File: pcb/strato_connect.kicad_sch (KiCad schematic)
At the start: 42 parts, among them J1 Conn_Coaxial, J2 Conn_02x03_Odd_Even, J3 Conn_01x04_Pin, J4 Conn_01x02_Pin, J5 Conn_01x05_Pin, SW1 SW_SPST, SW2 SW_SPST, U1 TPS565242, U2 ATmega328PB-A, U4 RF4463F30, Y1 CSTNE16M0V530000R0

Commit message: rough layout of the rev2 pcb
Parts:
- removed U2: ATmega328PB-A, Package_QFP:TQFP-32_7x7mm_P0.8mm, symbol MCU_Microchip_ATmega:ATmega328PB-A
- added U2: ATmega328PB-M, Package_DFN_QFN:QFN-32-1EP_5x5mm_P0.5mm_EP3.1x3.1mm, symbol MCU_Microchip_ATmega:ATmega328PB-M
- C11, C9: footprint Capacitor_SMD:CP_Elec_5x5.3 -> Capacitor_SMD:C_0603_1608Metric
- J2: footprint Connector_PinHeader_2.54mm:PinHeader_2x03_P2.54mm_Vertical -> Connector_PinHeader_2.54mm:PinHeader_2x03_P2.54mm_Vertical_SMD
- J3: footprint (none) -> Connector_JST:JST_SH_SM04B-SRSS-TB_1x04-1MP_P1.00mm_Horizontal
- J4: footprint Connector_JST:JST_SH_BM04B-SRSS-TB_1x04-1MP_P1.00mm_Vertical -> Connector_JST:JST_PH_S2B-PH-SM4-TB_1x02-1MP_P2.00mm_Horizontal
- J5: footprint (none) -> Connector_JST:JST_SH_SM05B-SRSS-TB_1x05-1MP_P1.00mm_Horizontal
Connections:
- net +5V: now also U2.18 (AVCC), U2.20 (AREF), U2.4 (VCC)
- net GND: now also U2.21 (GND), U2.33 (GND), U2.5 (GND)
- net LED_RX: now also U2.25 (PC2)
- net LED_TX: now also U2.26 (PC3)
- net SCL: now also U2.28 (PC5)
- net SDA: now also U2.27 (PC4)
- net SPI_MISO: now also U2.16 (PB4)
- net SPI_MOSI: now also U2.15 (PB3)
- net SPI_SCK: now also U2.17 (PB5)
- net ~{INT}: now also U2.24 (PC1)
- net ~{IRQ}: now also U2.32 (PD2)
- net ~{RST}: now also U2.29 (~{RESET}/PC6)
- net ~{SDN}: now also U2.13 (PB1)
- net ~{SPI_CS}: now also U2.14 (PB2)
- net ~{TRIG}: now also U2.1 (PD3)
- net at R2.1: now also U2.31 (PD1)
- net at Y1.1: now also U2.8 (XTAL2/PB7)
- net at Y1.3: now also U2.7 (XTAL1/PB6)
- net at R1.1: now also U2.30 (PD0)
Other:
- moved on the sheet: C1, C10, C2, C4, R1, R2, Y1

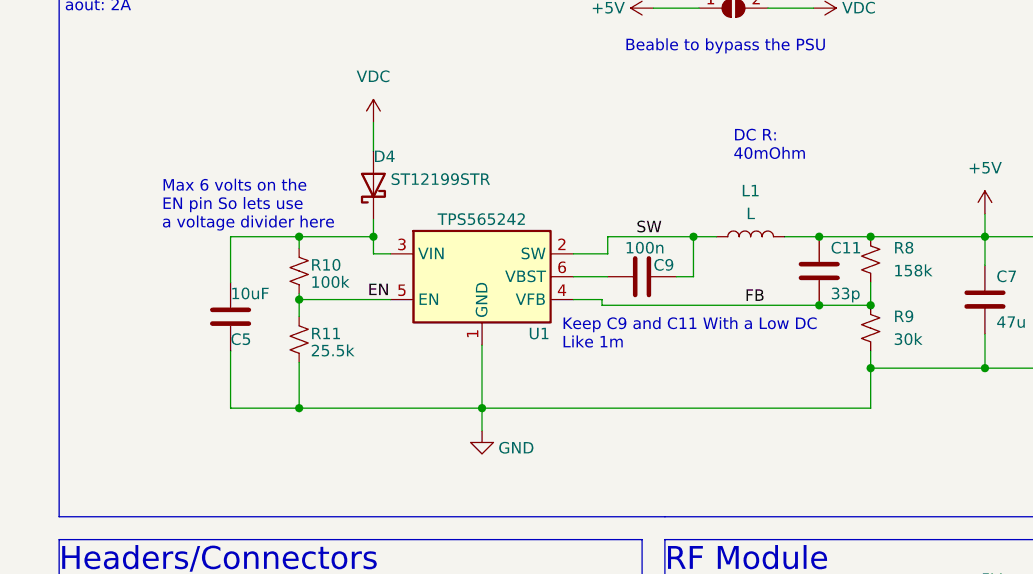
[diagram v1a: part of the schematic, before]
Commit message: get most of the layout done, need to add some sort of icsp header pins
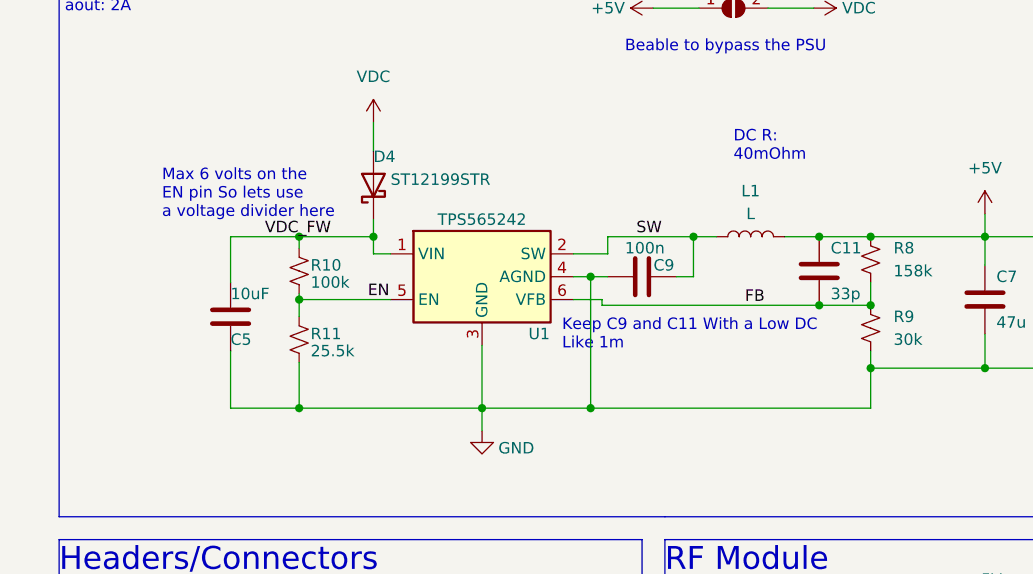
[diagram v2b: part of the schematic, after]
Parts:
- R10, R11, R8, R9: footprint Resistor_SMD:R_0805_2012Metric -> Resistor_SMD:R_0402_1005Metric_Pad0.72x0.64mm_HandSolder
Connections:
- net FB: now also U1.6 (VFB); no longer U1.4 (VFB)
- net GND: now also C9.2, U1.3 (GND), U1.4 (AGND); no longer U1.1 (GND)
- net VDC_FW: now reaches C5.1, D4.1 (K), R10.1
- net VDC_FW: now also U1.1 (VIN); no longer U1.3 (VIN)
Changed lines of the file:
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@@
   (junction (at 242.57 49.53) (diameter 0) (color 0 0 0 0)
+  )
+  (junction (at 198.755 53.975) (diameter 0) (color 0 0 0 0)
+  )
+  (junction (at 198.755 68.58) (diameter 0) (color 0 0 0 0)
   )
   (junction (at 166.37 49.53) (diameter 0) (color 0 0 0 0)
@@
     (stroke (width 0) (type default))
   )
+  (wire (pts (xy 198.755 53.975) (xy 200.66 53.975))
+    (stroke (width 0) (type default))
+  )
   (wire (pts (xy 259.08 115.57) (xy 266.065 115.57))
     (stroke (width 0) (type default))
@@
     (stroke (width 0) (type default))
   )
-  (wire (pts (xy 196.85 53.975) (xy 200.66 53.975))
+  (wire (pts (xy 196.85 53.975) (xy 198.755 53.975))
     (stroke (width 0) (type default))
   )
@@
     (stroke (width 0) (type default))
   )
-  (wire (pts (xy 186.69 68.58) (xy 229.87 68.58))
+  (wire (pts (xy 186.69 68.58) (xy 198.755 68.58))
     (stroke (width 0) (type default))
   )
@@
     (stroke (width 0) (type default))
   )
+  (wire (pts (xy 198.755 53.975) (xy 198.755 68.58))
+    (stroke (width 0) (type default))
+  )
   (wire (pts (xy 259.08 113.03) (xy 259.08 115.57))
     (stroke (width 0) (type default))
@@
   )
   (wire (pts (xy 166.37 56.515) (xy 176.53 56.515))
+    (stroke (width 0) (type default))
+  )
+  (wire (pts (xy 198.755 68.58) (xy 229.87 68.58))
     (stroke (width 0) (type default))
   )
@@
   )
   (text "Max 6 volts on the\nEN pin So lets use \na voltage divider here"
-    (at 151.13 48.895 0)
+    (at 151.13 47.625 0)
     (effects (font (size 1.27 1.27)) (justify left bottom))
   )
@@
   )
   (text "Beable to bypass the PSU" (at 202.565 29.21 0)
+    (effects (font (size 1.27 1.27)) (justify left bottom))
+  )
+  (label "VDC_FW" (at 162.56 49.53 0) (fields_autoplaced)
     (effects (font (size 1.27 1.27)) (justify left bottom))
   )
@@
       (effects (font (size 1.27 1.27)) (justify left))
     )
-    (property "Footprint" "Resistor_SMD:R_0805_2012Metric" (at 166.37 60.96 0)
+    (property "Footprint" "Resistor_SMD:R_0402_1005Metric_Pad0.72x0.64mm_HandSolder" (at 166.37 60.96 0)
       (effects (font (size 1.27 1.27)) hide)
     )
@@
       (effects (font (size 1.27 1.27)) (justify left))
     )
-    (property "Footprint" "Resistor_SMD:R_0805_2012Metric" (at 229.87 52.07 0)
+    (property "Footprint" "Resistor_SMD:R_0402_1005Metric_Pad0.72x0.64mm_HandSolder" (at 229.87 52.07 0)
       (effects (font (size 1.27 1.27)) hide)
     )
@@
       (effects (font (size 1.27 1.27)) (justify left))
     )
-    (property "Footprint" "Resistor_SMD:R_0805_2012Metric" (at 166.37 53.34 0)
+    (property "Footprint" "Resistor_SMD:R_0402_1005Metric_Pad0.72x0.64mm_HandSolder" (at 166.37 53.34 0)
       (effects (font (size 1.27 1.27)) hide)
     )
@@
       (effects (font (size 1.27 1.27)) (justify left))
     )
-    (property "Footprint" "Resistor_SMD:R_0805_2012Metric" (at 229.87 59.69 0)
-      (effects (font (size 1.27 1.27)) hide)
-    )
+    (property "Footprint" "Resistor_SMD:R_0402_1005Metric_Pad0.72x0.64mm_HandSolder" (at 229.87 59.69 0)
+      (effects (font (size 1.27 1.27)) hide)
+    )

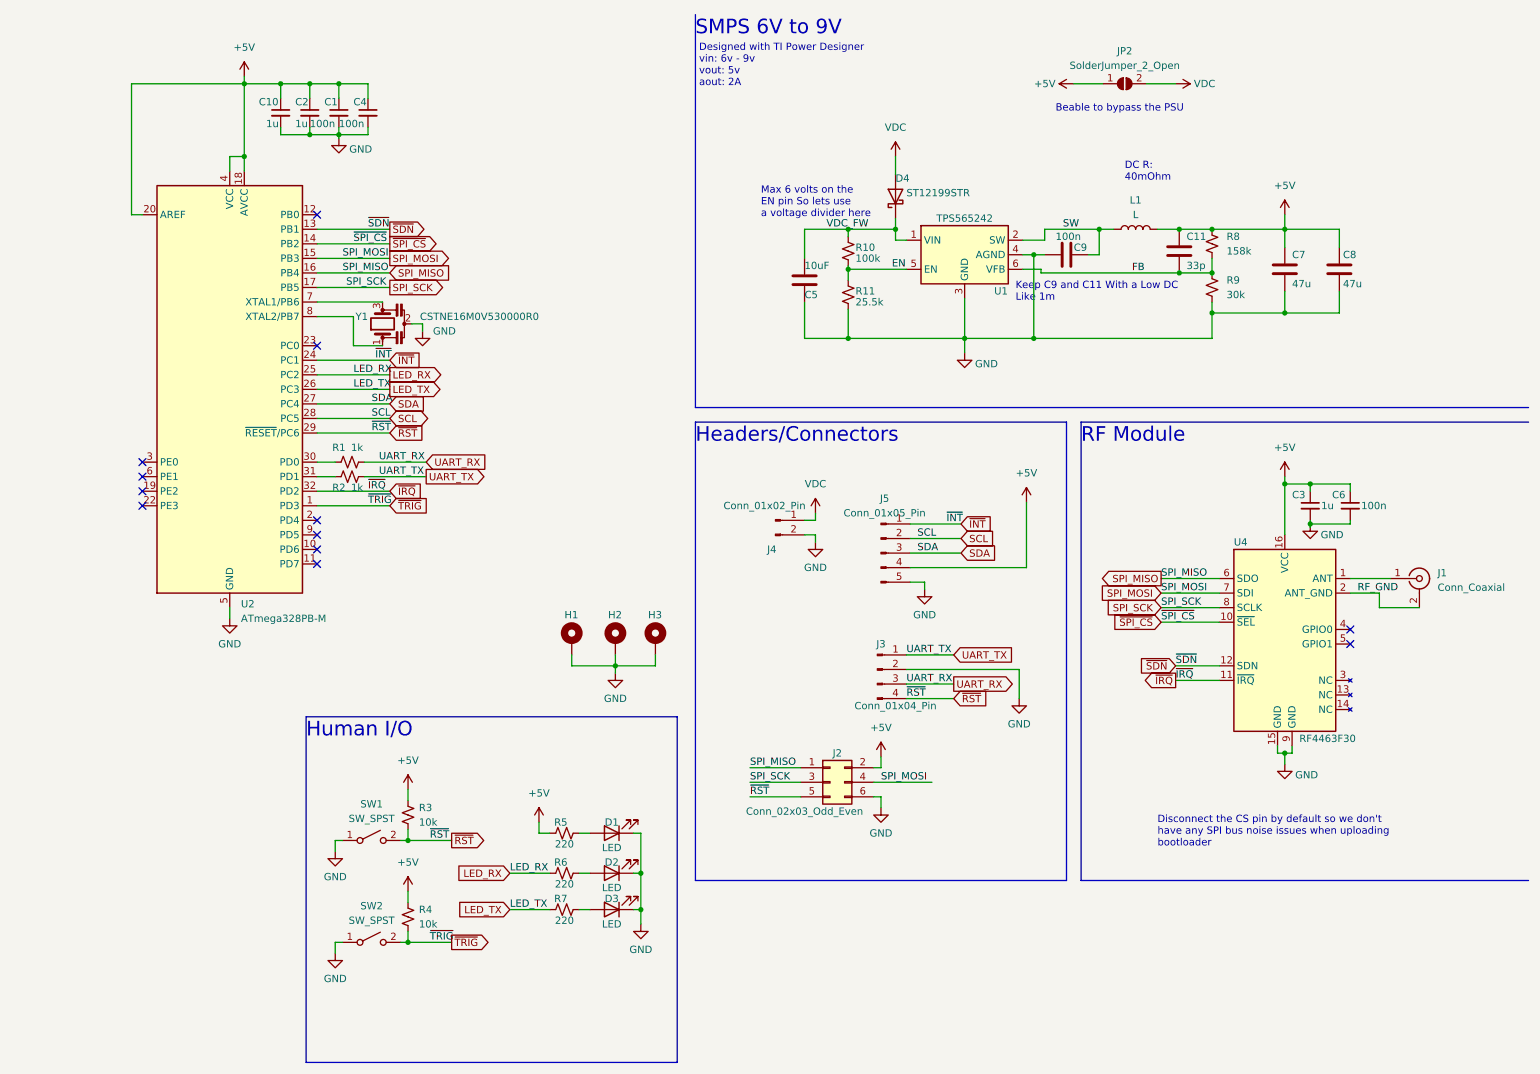
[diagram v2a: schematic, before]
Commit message: pass DRC with the schematic capture
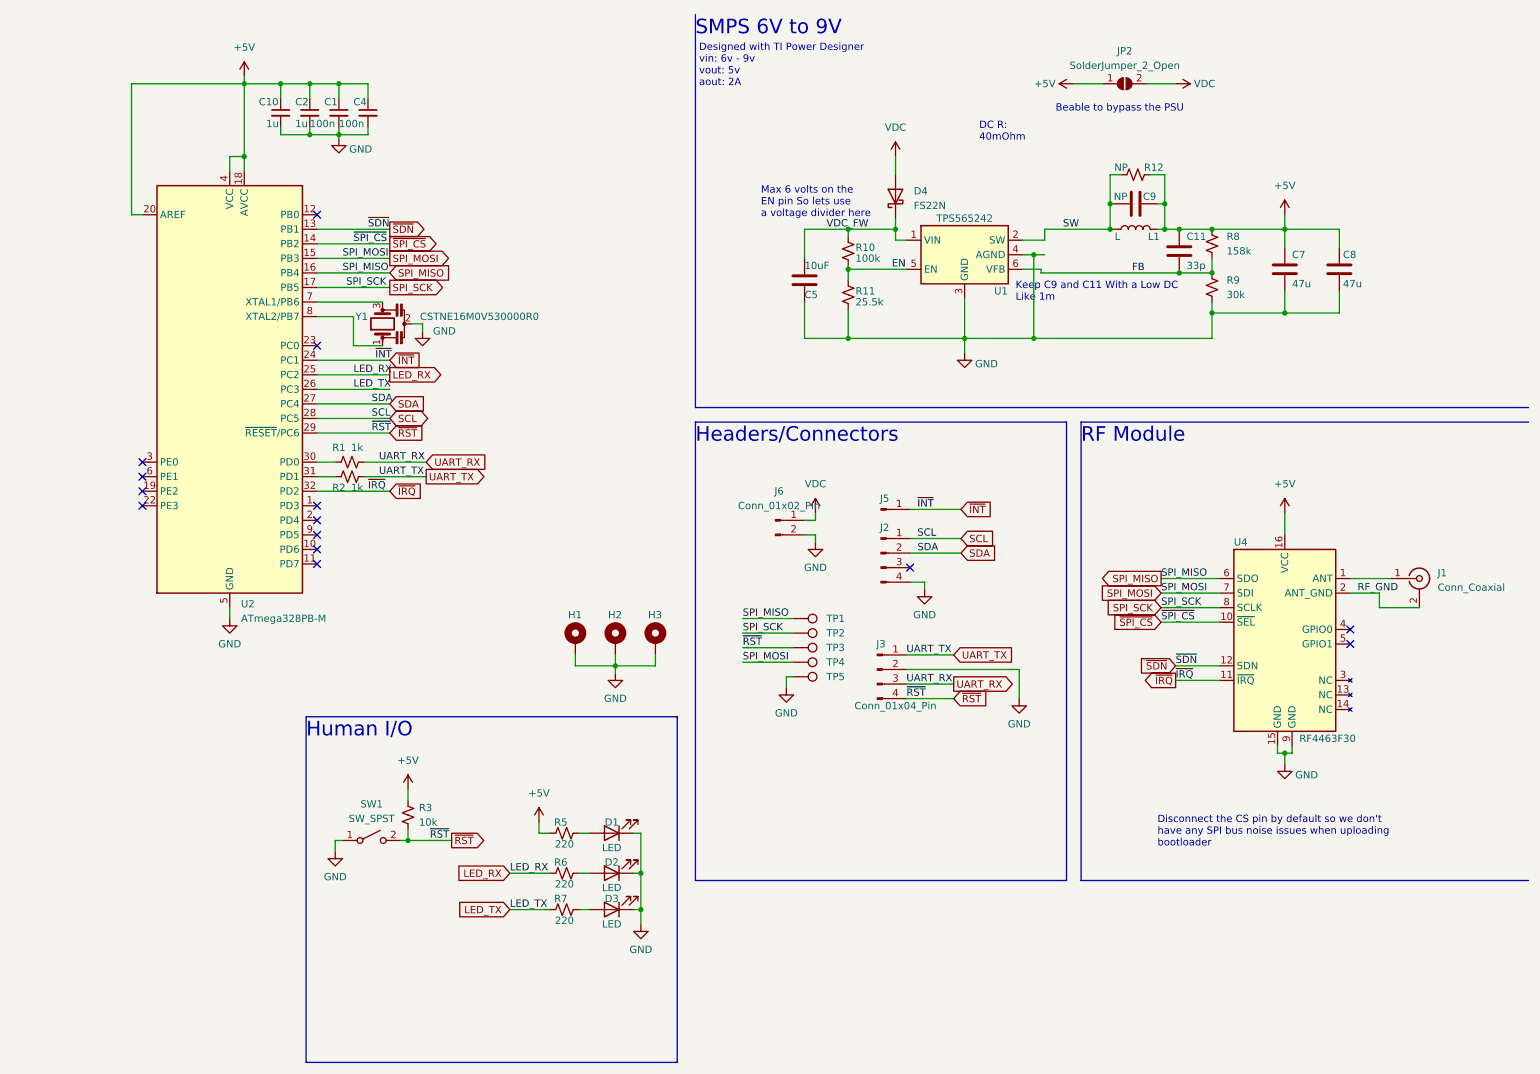
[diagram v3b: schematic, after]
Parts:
- removed C3: 1u, Capacitor_SMD:C_0603_1608Metric, symbol Device:C_Small
- removed C6: 100n, Capacitor_SMD:C_0603_1608Metric, symbol Device:C_Small
- removed D4: ST12199STR, Kevin_Lutzer_Lbr:Diode-TO-277B, symbol Kevin_Lutzer_Lbr:ST12199STR
- removed J2: Conn_02x03_Odd_Even, Connector_PinHeader_2.54mm:PinHeader_2x03_P2.54mm_Vertical_SMD, symbol Connector_Generic:Conn_02x03_Odd_Even
- removed J4: Conn_01x02_Pin, Connector_JST:JST_PH_S2B-PH-SM4-TB_1x02-1MP_P2.00mm_Horizontal, symbol Connector:Conn_01x02_Pin
- removed J5: Conn_01x05_Pin, Connector_JST:JST_SH_SM05B-SRSS-TB_1x05-1MP_P1.00mm_Horizontal, symbol Connector:Conn_01x05_Pin
- removed R4: 10k, Resistor_SMD:R_0603_1608Metric, symbol Device:R_Small_US
- removed SW2: SW_SPST, Button_Switch_SMD:SW_Push_1P1T_NO_CK_KMR2, symbol Switch:SW_SPST
- added D4: FS22N, Diode_SMD:D_SOD-123F, symbol Kevin_Lutzer_Lbr:FS22N
- added J2: Conn_01x04_Pin, Connector_JST:JST_SH_SM04B-SRSS-TB_1x04-1MP_P1.00mm_Horizontal, symbol Connector:Conn_01x04_Pin
- added J5: Conn_01x01_Pin, TestPoint:TestPoint_Keystone_5019_Minature, symbol Connector:Conn_01x01_Pin
- added J6: Conn_01x02_Pin, Connector_JST:JST_PH_S2B-PH-SM4-TB_1x02-1MP_P2.00mm_Horizontal, symbol Connector:Conn_01x02_Pin
- added R12: NP, Resistor_SMD:R_0402_1005Metric_Pad0.72x0.64mm_HandSolder, symbol Device:R_Small_US
- added TP1, TP2, TP3, TP4, TP5: TestPoint, TestPoint:TestPoint_THTPad_D1.0mm_Drill0.5mm, symbol Connector:TestPoint
- C1, C10, C11, C2, C4: footprint Capacitor_SMD:C_0603_1608Metric -> Capacitor_SMD:C_0402_1005Metric_Pad0.74x0.62mm_HandSolder
- C5: footprint Capacitor_SMD:C_0805_2012Metric -> Capacitor_SMD:C_0603_1608Metric_Pad1.08x0.95mm_HandSolder
- C9: value 100n -> NP; footprint Capacitor_SMD:C_0603_1608Metric -> Capacitor_SMD:C_0402_1005Metric_Pad0.74x0.62mm_HandSolder
- R1, R2, R3, R6, R7: footprint Resistor_SMD:R_0603_1608Metric -> Resistor_SMD:R_0402_1005Metric_Pad0.72x0.64mm_HandSolder
- R5: footprint Resistor_SMD:R_0603_1608Metric -> Resistor_SMD:R_0603_1608Metric_Pad0.98x0.95mm_HandSolder
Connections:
- net +5V: now also C9.1, R12.2
- net GND: now also J2.4 (Pin_4), J6.2 (Pin_2), TP5.1; no longer C9.2
- net SCL: now also J2.1 (Pin_1)
- net SDA: now also J2.2 (Pin_2)
- net SPI_MISO: now also TP1.1
- net SPI_MOSI: now also TP4.1
- net SPI_SCK: now also TP2.1
- net SW: now also C9.2, R12.1; no longer C9.1
- net VDC: now also D4.2 (A), J6.1 (Pin_1)
- net VDC_FW: now also D4.1 (K)
- net ~{INT}: now also J5.1 (Pin_1)
- net ~{RST}: now also TP3.1
- net ~{TRIG}: no longer names the net of U2.1 (PD3)
- no-connect marks 12 -> 14
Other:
- moved on the sheet: C9, H1

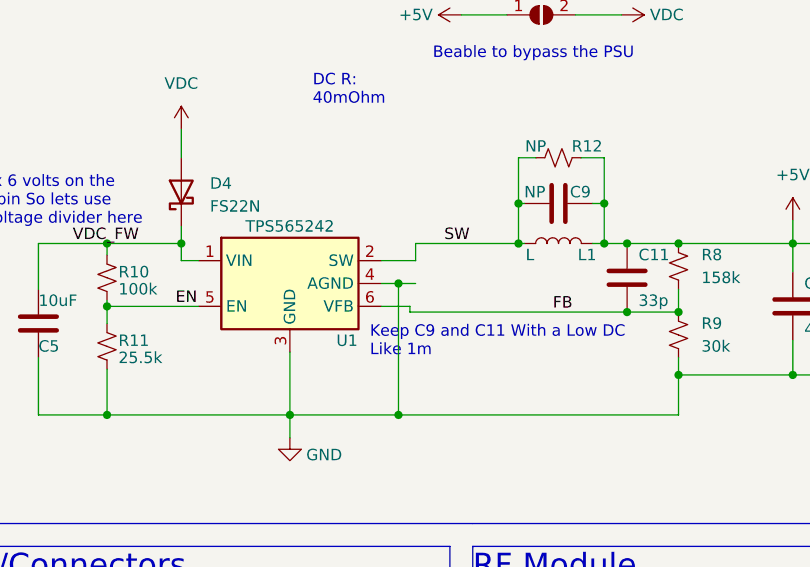
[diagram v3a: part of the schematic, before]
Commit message: add the 4025 Weurth inductor footprint in
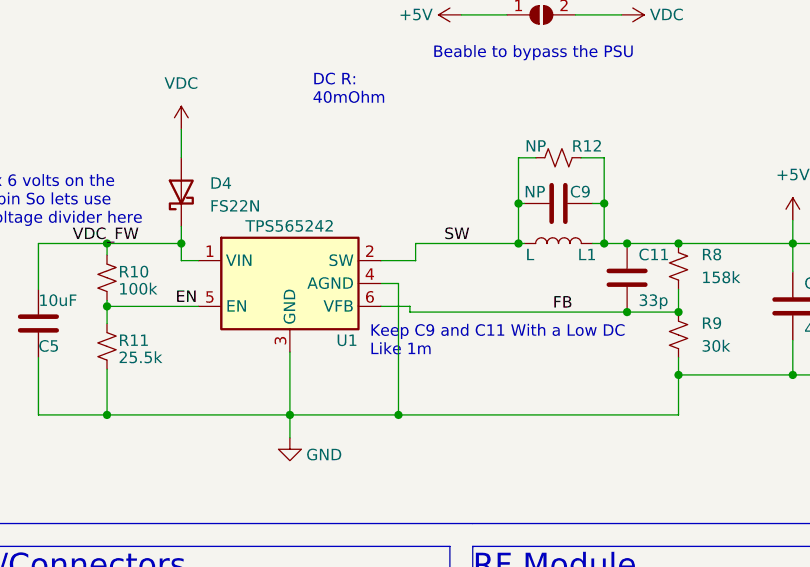
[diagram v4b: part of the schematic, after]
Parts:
- L1: footprint Inductor_SMD_Wurth:L_Wurth_WE-LQSH-4020 -> Kevin_Lutzer_Lbr:L_Wurth_WE-LQSH-4025
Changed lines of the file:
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@@
   (junction (at 212.09 49.53) (diameter 0) (color 0 0 0 0)
-  )
-  (junction (at 198.755 53.975) (diameter 0) (color 0 0 0 0)
   )
   (junction (at 198.755 68.58) (diameter 0) (color 0 0 0 0)
@@
   )
   (polyline (pts (xy 207.01 80.645) (xy 139.7 80.645))
-    (stroke (width 0) (type default))
-  )
-  (wire (pts (xy 198.755 53.975) (xy 200.66 53.975))
     (stroke (width 0) (type default))
   )
@@
       (effects (font (size 1.27 1.27)))
     )
-    (property "Footprint" "Inductor_SMD_Wurth:L_Wurth_WE-LQSH-4020" (at 216.535 49.53 0)
-      (effects (font (size 1.27 1.27)) hide)
-    )
+    (property "Footprint" "Kevin_Lutzer_Lbr:L_Wurth_WE-LQSH-4025" (at 216.535 49.53 0)
+      (effects (font (size 1.27 1.27)) hide)
+    )

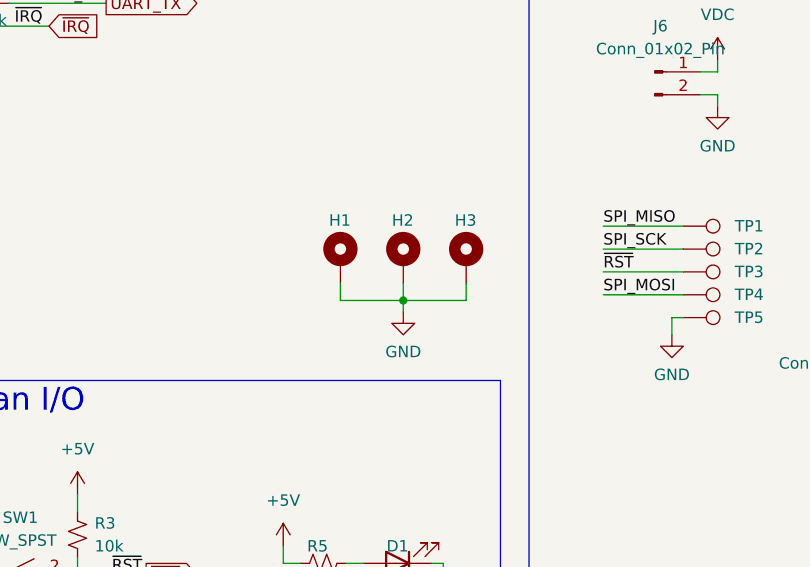
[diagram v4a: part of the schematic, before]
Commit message: pass drc rules for files, just have to add the silk screen
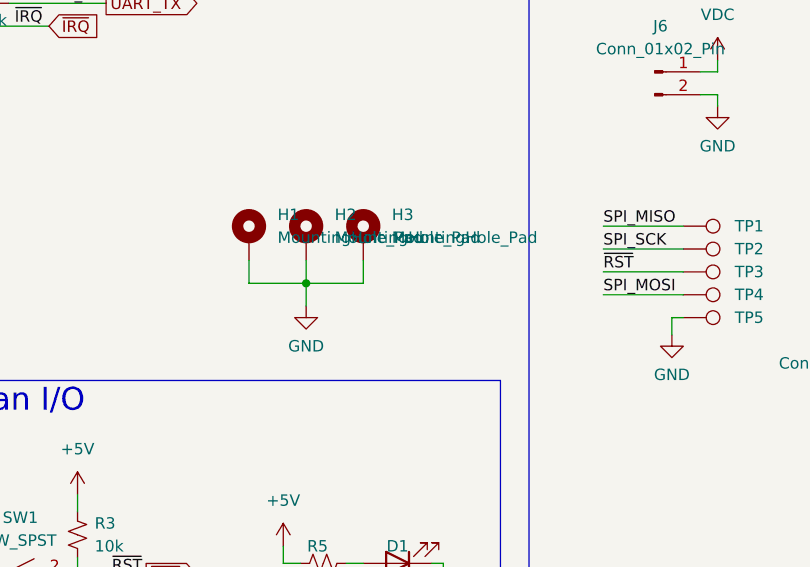
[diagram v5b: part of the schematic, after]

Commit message: Switch the coax connector type
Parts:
- J1: footprint Connector_Coaxial:SMA_Amphenol_901-143_Horizontal -> Connector_Coaxial:SMA_Wurth_60312002114503_Vertical
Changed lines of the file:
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@@
       (effects (font (size 1.27 1.27)) (justify left))
     )
-    (property "Footprint" "Connector_Coaxial:SMA_Amphenol_901-143_Horizontal" (at 266.065 110.49 0)
+    (property "Footprint" "Connector_Coaxial:SMA_Wurth_60312002114503_Vertical" (at 266.065 110.49 0)
       (effects (font (size 1.27 1.27)) hide)
     )
